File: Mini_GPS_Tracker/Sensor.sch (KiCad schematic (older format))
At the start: 16 parts, among them U1 ADXL343, U2 MS5611-01BA, U7 BNO055, Y2 32.7568KHz

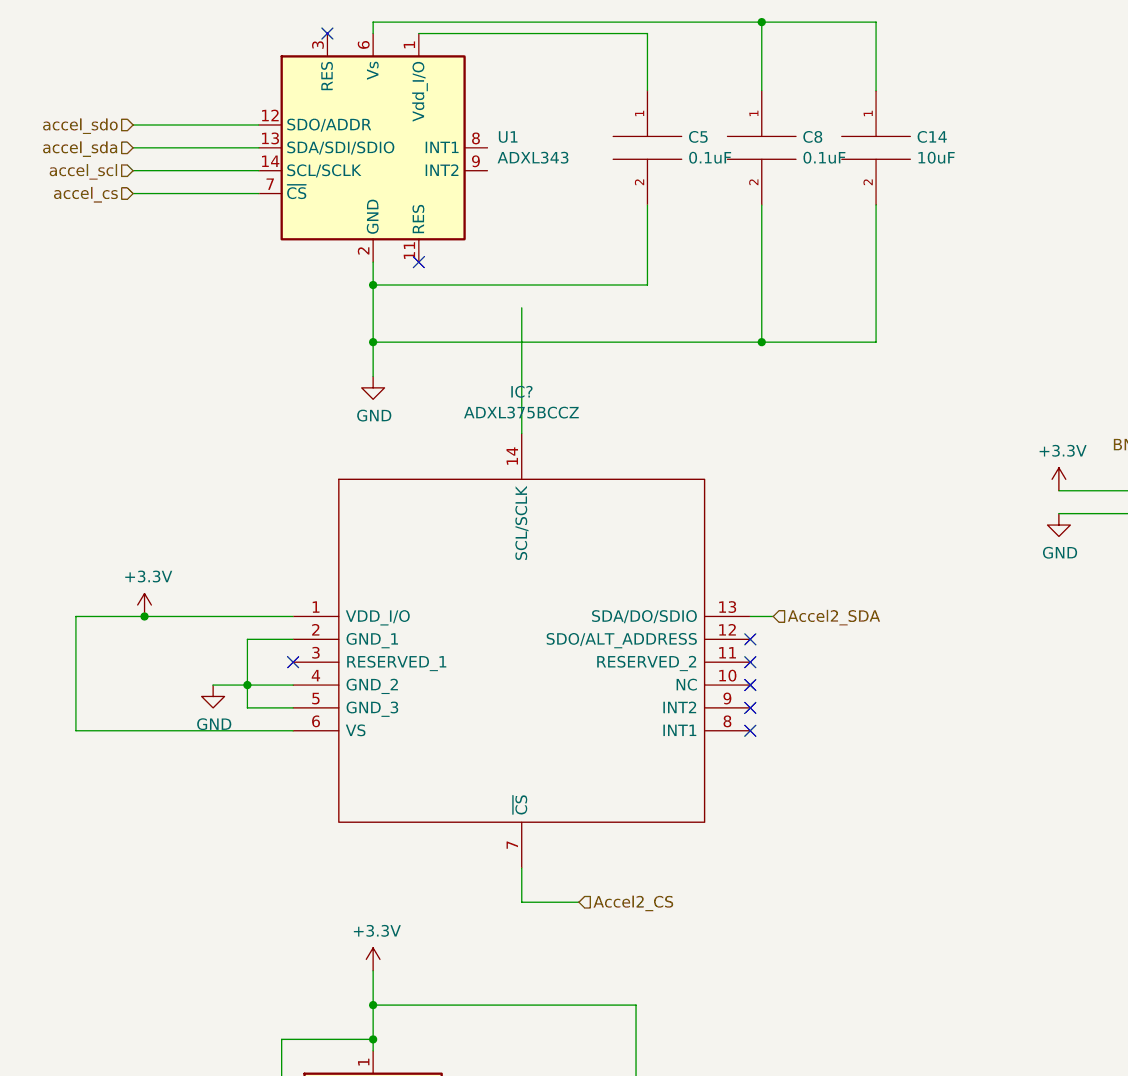
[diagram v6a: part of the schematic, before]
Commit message: Add files via upload
Splitting board into modules
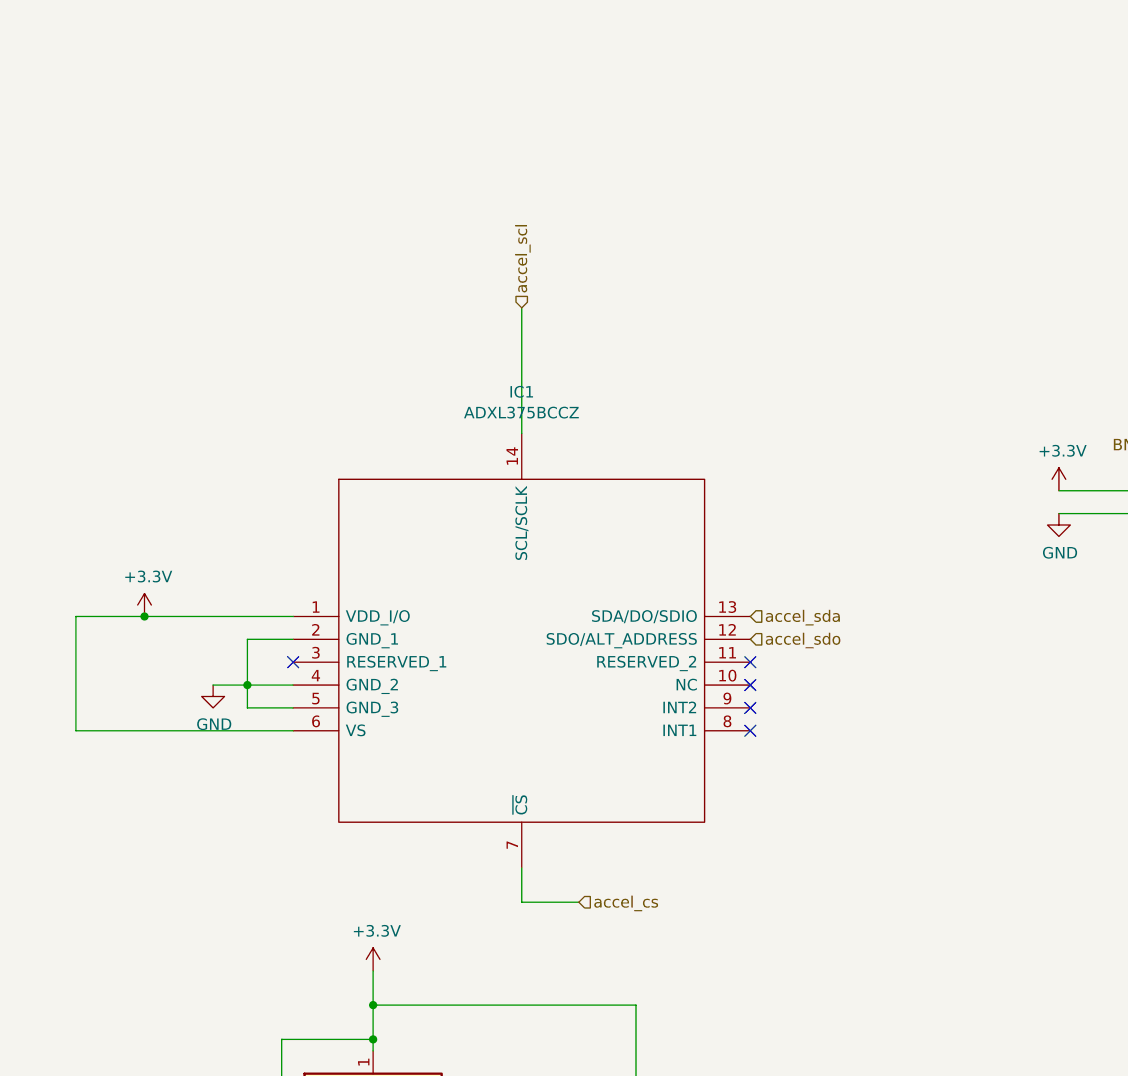
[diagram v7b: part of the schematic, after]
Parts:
- removed C14: 10uF, Capacitor_SMD:C_0805_2012Metric_Pad1.15x1.40mm_HandSolder, symbol pspice:CAP
- removed C5, C8: 0.1uF, Capacitor_SMD:C_0805_2012Metric_Pad1.15x1.40mm_HandSolder, symbol pspice:CAP
- removed U1: ADXL343, Package_LGA:LGA-14_3x5mm_P0.8mm_LayoutBorder1x6y, symbol Sensor_Motion:ADXL343
- gave numbers to parts that had none: 1
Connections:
- net Accel2_CS is gone; now on net accel_cs: IC1.7 (~CS)
- net Accel2_SDA is gone; now on net accel_sda: IC1.13 (SDA/DO/SDIO)
- net accel_scl: now also IC1.14 (SCL/SCLK)
- net accel_sdo: now also IC1.12 (SDO/ALT_ADDRESS)
- no-connect marks 10 -> 7
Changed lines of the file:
@@
 $Descr A4 11693 8268
 encoding utf-8
-Sheet 2 7
+Sheet 2 13
 Title ""
 Date ""
@@
 	1    0    0    -1
 $EndComp
-$Comp
-L Sensor_Motion:ADXL343 U1
-U 1 1 5E8940BD
-P 2500 1950
-F 0 "U1" H 3044 1996 50  0000 L CNN
-F 1 "ADXL343" H 3044 1905 50  0000 L CNN
-F 2 "Package_LGA:LGA-14_3x5mm_P0.8mm_LayoutBorder1x6y" H 2500 1950 50  0001 C CNN
-F 3 "https://www.analog.com/media/en/technical-documentation/data-sheets/ADXL343.pdf" H 2500 1950 50  0001 C CNN
-	1    2500 1950
-	1    0    0    -1
-$EndComp
-$Comp
-L power:GND #PWR0117
-U 1 1 5E8951BC
-P 2500 2950
-F 0 "#PWR0117" H 2500 2700 50  0001 C CNN
-F 1 "GND" H 2505 2777 50  0000 C CNN
-F 2 "" H 2500 2950 50  0001 C CNN
-F 3 "" H 2500 2950 50  0001 C CNN
-	1    2500 2950
-	1    0    0    -1
-$EndComp
-Wire Wire Line
-	2500 2450 2500 2550
-Text HLabel 1450 2150 0    50   Input ~ 0
+Text HLabel 3400 5250 2    50   Input ~ 0
 accel_cs
-Text HLabel 1450 2050 0    50   Input ~ 0
+Text HLabel 3150 2650 1    50   Input ~ 0
 accel_scl
-Text HLabel 1450 1950 0    50   Input ~ 0
-accel_sda
-Text HLabel 1450 1850 0    50   Input ~ 0
-accel_sdo
-Wire Wire Line
-	1450 2050 2000 2050
-Wire Wire Line
-	1450 2150 2000 2150
-Wire Wire Line
-	1450 1950 2000 1950
-Wire Wire Line
-	1450 1850 2000 1850
-$Comp
-L pspice:CAP C5
-U 1 1 5E89F2A3
-P 3700 1950
-F 0 "C5" H 3878 1996 50  0000 L CNN
-F 1 "0.1uF" H 3878 1905 50  0000 L CNN
-F 2 "Capacitor_SMD:C_0805_2012Metric_Pad1.15x1.40mm_HandSolder" H 3700 1950 50  0001 C CNN
-F 3 "~" H 3700 1950 50  0001 C CNN
-	1    3700 1950
-	1    0    0    -1
-$EndComp
-$Comp
-L pspice:CAP C8
-U 1 1 5E89F917
-P 4200 1950
-F 0 "C8" H 4378 1996 50  0000 L CNN
-F 1 "0.1uF" H 4378 1905 50  0000 L CNN
-F 2 "Capacitor_SMD:C_0805_2012Metric_Pad1.15x1.40mm_HandSolder" H 4200 1950 50  0001 C CNN
-F 3 "~" H 4200 1950 50  0001 C CNN
-	1    4200 1950
-	1    0    0    -1
-$EndComp
-Wire Wire Line
-	2700 1450 3700 1450
-Wire Wire Line
-	3700 1450 3700 1700
-Wire Wire Line
-	3700 2200 3700 2550
-Wire Wire Line
-	3700 2550 2500 2550
-Connection ~ 2500 2550
-Wire Wire Line
-	2500 2550 2500 2800
-$Comp
-L pspice:CAP C14
-U 1 1 5E8A3F23
-P 4700 1950
-F 0 "C14" H 4878 1996 50  0000 L CNN
-F 1 "10uF" H 4878 1905 50  0000 L CNN
-F 2 "Capacitor_SMD:C_0805_2012Metric_Pad1.15x1.40mm_HandSolder" H 4700 1950 50  0001 C CNN
-F 3 "~" H 4700 1950 50  0001 C CNN
-	1    4700 1950
-	1    0    0    -1
-$EndComp
-Wire Wire Line
-	2500 2800 4200 2800
-Wire Wire Line
-	4700 2800 4700 2200
-Connection ~ 2500 2800
-Wire Wire Line
-	2500 2800 2500 2950
-Wire Wire Line
-	4200 2200 4200 2800
-Connection ~ 4200 2800
-Wire Wire Line
-	4200 2800 4700 2800
-Wire Wire Line
-	2500 1400 4200 1400
-Wire Wire Line
-	4700 1400 4700 1700
-Wire Wire Line
-	2500 1400 2500 1450
-Wire Wire Line
-	4200 1700 4200 1400
-Connection ~ 4200 1400
-Wire Wire Line
-	4200 1400 4700 1400
-NoConn ~ 2300 1450
-NoConn ~ 2700 2450
+Wire Wire Line
+	3150 2650 3150 3200
 $Comp
 L power:GND #PWR0118
@@
 Wire Wire Line
 	7100 3550 5500 3550
-Text HLabel 4250 4000 2    50   Input ~ 0
-Accel2_SDA
-Wire Wire Line
-	4250 4000 4150 4000
 $Comp
 L SamacSys_Parts:ADXL375BCCZ IC?
@@
 P 2150 4000
 AR Path="/5E9E34E6/5EB47FDF" Ref="IC?"  Part="1"
-AR Path="/5E70BD5E/5EB47FDF" Ref="IC?"  Part="1"
-F 0 "IC?" H 3150 4981 50  0000 C CNN
+AR Path="/5E70BD5E/5EB47FDF" Ref="IC1"  Part="1"
+F 0 "IC1" H 3150 4981 50  0000 C CNN
 F 1 "ADXL375BCCZ" H 3150 4890 50  0000 C CNN
 F 2 "CC-14-1" H 4000 4600 50  0001 L CNN
@@
 $EndComp
 Wire Wire Line
-	3150 2650 3150 3200
-Wire Wire Line
 	2150 4100 1950 4100
 Wire Wire Line
@@
 P 1800 4300
 AR Path="/5E9E34E6/5EB47FEC" Ref="#PWR?"  Part="1"
-AR Path="/5E70BD5E/5EB47FEC" Ref="#PWR?"  Part="1"
-F 0 "#PWR?" H 1800 4050 50  0001 C CNN
+AR Path="/5E70BD5E/5EB47FEC" Ref="#PWR013"  Part="1"
+F 0 "#PWR013" H 1800 4050 50  0001 C CNN
 F 1 "GND" H 1805 4127 50  0000 C CNN
 F 2 "" H 1800 4300 50  0001 C CNN
@@
 P 1500 4000
 AR Path="/5E9E34E6/5EB47FF6" Ref="#PWR?"  Part="1"
-AR Path="/5E70BD5E/5EB47FF6" Ref="#PWR?"  Part="1"
-F 0 "#PWR?" H 1500 3850 50  0001 C CNN
+AR Path="/5E70BD5E/5EB47FF6" Ref="#PWR010"  Part="1"
+F 0 "#PWR010" H 1500 3850 50  0001 C CNN
 F 1 "+3.3V" H 1515 4173 50  0000 C CNN
 F 2 "" H 1500 4000 50  0001 C CNN
@@
 NoConn ~ 4150 4500
 NoConn ~ 2150 4200
-Text HLabel 3400 5250 2    50   Input ~ 0
-Accel2_CS
 Wire Wire Line
 	3150 5100 3150 5250
 Wire Wire Line
 	3150 5250 3400 5250
-NoConn ~ 4150 4100
 NoConn ~ 4150 4200
+Text HLabel 4150 4000 2    50   Input ~ 0
+accel_sda
+Text HLabel 4150 4100 2    50   Input ~ 0
+accel_sdo
 $EndSCHEMATC
